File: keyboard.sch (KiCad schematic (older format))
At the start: 80 parts

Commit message: Switch to STM32, wire stuff
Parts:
- gave numbers to parts that had none: 80
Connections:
- net KB_ROW_5: now reaches SW3.1
- net KB_ROW_5: now also SW12.1, SW17.1, SW2.1, SW22.1, SW26.1, SW34.1, SW39.1, SW44.1, SW51.1, SW59.1, SW66.1, SW76.1
- net KB_COL_2: now reaches SW3.2
- net KB_COL_2: now also SW10.2, SW11.2, SW8.2, SW9.2
- net KB_COL_3: now reaches SW12.2
- net KB_COL_3: now also SW13.2, SW14.2, SW15.2, SW16.2
- net KB_COL_4: now reaches SW17.2
- net KB_COL_4: now also SW18.2, SW19.2, SW20.2, SW21.2
- net KB_COL_5: now reaches SW22.2
- net KB_COL_5: now also SW23.2, SW24.2, SW25.2
- net KB_COL_6: now reaches SW26.2
- net KB_COL_6: now also SW27.2, SW28.2, SW29.2, SW30.2
- net KB_COL_7: now reaches SW34.2
- net KB_COL_7: now also SW31.2, SW32.2, SW33.2
- net KB_COL_8: now reaches SW39.2
- net KB_COL_8: now also SW35.2, SW36.2, SW37.2, SW38.2
- net KB_COL_9: now reaches SW44.2
- net KB_COL_9: now also SW40.2, SW41.2, SW42.2, SW43.2
- net KB_ROW_7: now reaches SW4.1
- net KB_ROW_7: now also SW13.1, SW18.1, SW23.1, SW27.1, SW31.1, SW35.1, SW40.1, SW45.1, SW53.1, SW61.1, SW68.1, SW78.1, SW8.1
- net KB_COL_1: now reaches SW4.2
- net KB_COL_1: now also SW2.2, SW5.2, SW6.2, SW7.2
- net KB_COL_10: now reaches SW45.2
- net KB_COL_10: now also SW46.2
- net KB_ROW_8: now reaches SW5.1
- net KB_ROW_8: now also SW14.1, SW19.1, SW24.1, SW28.1, SW32.1, SW36.1, SW41.1, SW54.1, SW62.1, SW69.1, SW79.1, SW9.1
- net KB_ROW_9: now reaches SW6.1
- net KB_ROW_9: now also SW10.1, SW15.1, SW20.1, SW25.1, SW29.1, SW33.1, SW37.1, SW42.1, SW46.1, SW55.1, SW63.1, SW70.1, SW80.1
- net KB_ROW_11: now reaches SW7.1
- net KB_ROW_10: now reaches SW11.1
- net KB_ROW_10: now also SW16.1, SW21.1, SW30.1, SW38.1, SW43.1, SW56.1, SW64.1, SW71.1, SW81.1
- net KB_COL_11: now reaches SW56.2
- net KB_COL_11: now also SW47.2, SW48.2, SW49.2, SW50.2, SW51.2, SW52.2, SW53.2, SW54.2, SW55.2
- net KB_COL_12: now reaches SW64.2
- net KB_COL_12: now also SW57.2, SW58.2, SW59.2, SW60.2, SW61.2, SW62.2, SW63.2
- net KB_COL_13: now reaches SW71.2
- net KB_COL_13: now also SW65.2, SW66.2, SW67.2, SW68.2, SW69.2, SW70.2, SW72.2, SW73.2, SW74.2
- net KB_COL_14: now reaches SW81.2
- net KB_COL_14: now also SW75.2, SW76.2, SW77.2, SW78.2, SW79.2, SW80.2
- net KB_ROW_6: now reaches SW52.1
- net KB_ROW_6: now also SW60.1, SW67.1, SW77.1
- net KB_ROW_4: now reaches SW50.1
- net KB_ROW_4: now also SW74.1
- net KB_ROW_3: now reaches SW49.1
- net KB_ROW_3: now also SW58.1, SW73.1
- net KB_ROW_2: now reaches SW75.1
- net KB_ROW_2: now also SW48.1, SW65.1
- net KB_ROW_1: now reaches SW57.1
- net KB_ROW_1: now also SW47.1, SW72.1
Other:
- note added: "ON button needs its own row for wakeup purpose"
- note removed: "10 cols / 8 rows ?"
- note removed: "ON button : wakeup possible on the ROW output ?\nin that case, 100kOhm pull-down to GND\n\n-> make ON on its own row"
- moved on the sheet: SW10, SW11, SW12, SW13, SW14, SW15, SW16, SW17, SW18, SW19, SW2, SW20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

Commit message: Some updates
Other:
- note removed: "total of 80 keys"
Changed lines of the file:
@@
 	1    0    0    -1
 $EndComp
-Text Notes 1500 6400 0    79   ~ 0
-total of 80 keys
 Text Notes 3450 6750 0    79   ~ 0
 COL are inputs, pull-up sw\nROW output
-Text Notes 1950 7050 0    118  ~ 0
-ON button needs its own row for wakeup purpose
 Text GLabel 1000 4500 0    50   Input ~ 0
 KB_ROW_8
@@
 Text GLabel 1000 5700 0    50   Input ~ 0
 KB_ROW_11
+Text Notes 1950 7050 0    118  ~ 0
+ON button needs its own row for wakeup purpose
 $EndSCHEMATC

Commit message: Assigning footprints
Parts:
- SW10, SW11, SW12, SW13, SW14, SW15, SW16, SW17, SW18, SW19, SW2, SW20, SW21, SW22, SW23, SW24, SW25, SW26, SW27, SW28, SW29, SW3, SW30, SW31, SW32, SW33, SW34, SW35, SW36, SW37, SW38, SW39, SW4, SW40, SW41, SW42, SW43, SW44, SW45, SW46, SW47, SW48, SW49, SW5, SW50, SW51, SW52, SW53, SW54, SW55, SW56, SW57, SW58, SW59, SW6, SW60, SW61, SW62, SW63, SW64, SW65, SW66, SW67, SW68, SW69, SW7, SW70, SW71, SW72, SW73, SW74, SW75, SW76, SW77, SW78, SW79, SW8, SW80, SW81, SW9: footprint (none) -> Button_Switch_THT:SW_PUSH_6mm

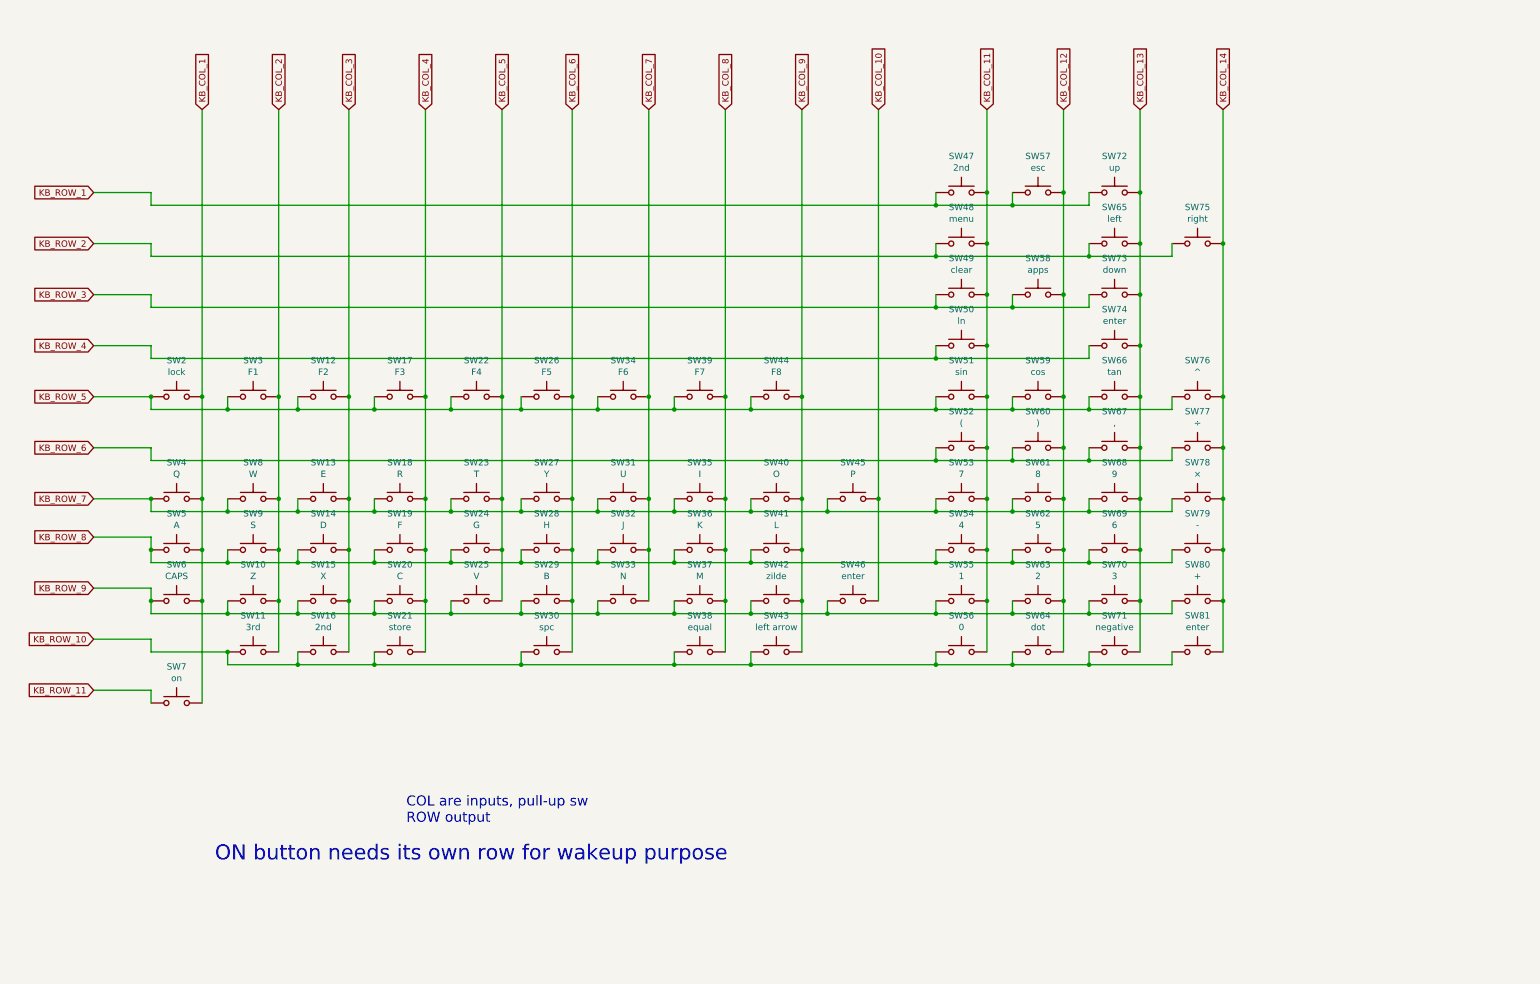
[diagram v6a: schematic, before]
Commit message: Switch keyboard matrix input to a mcp23017
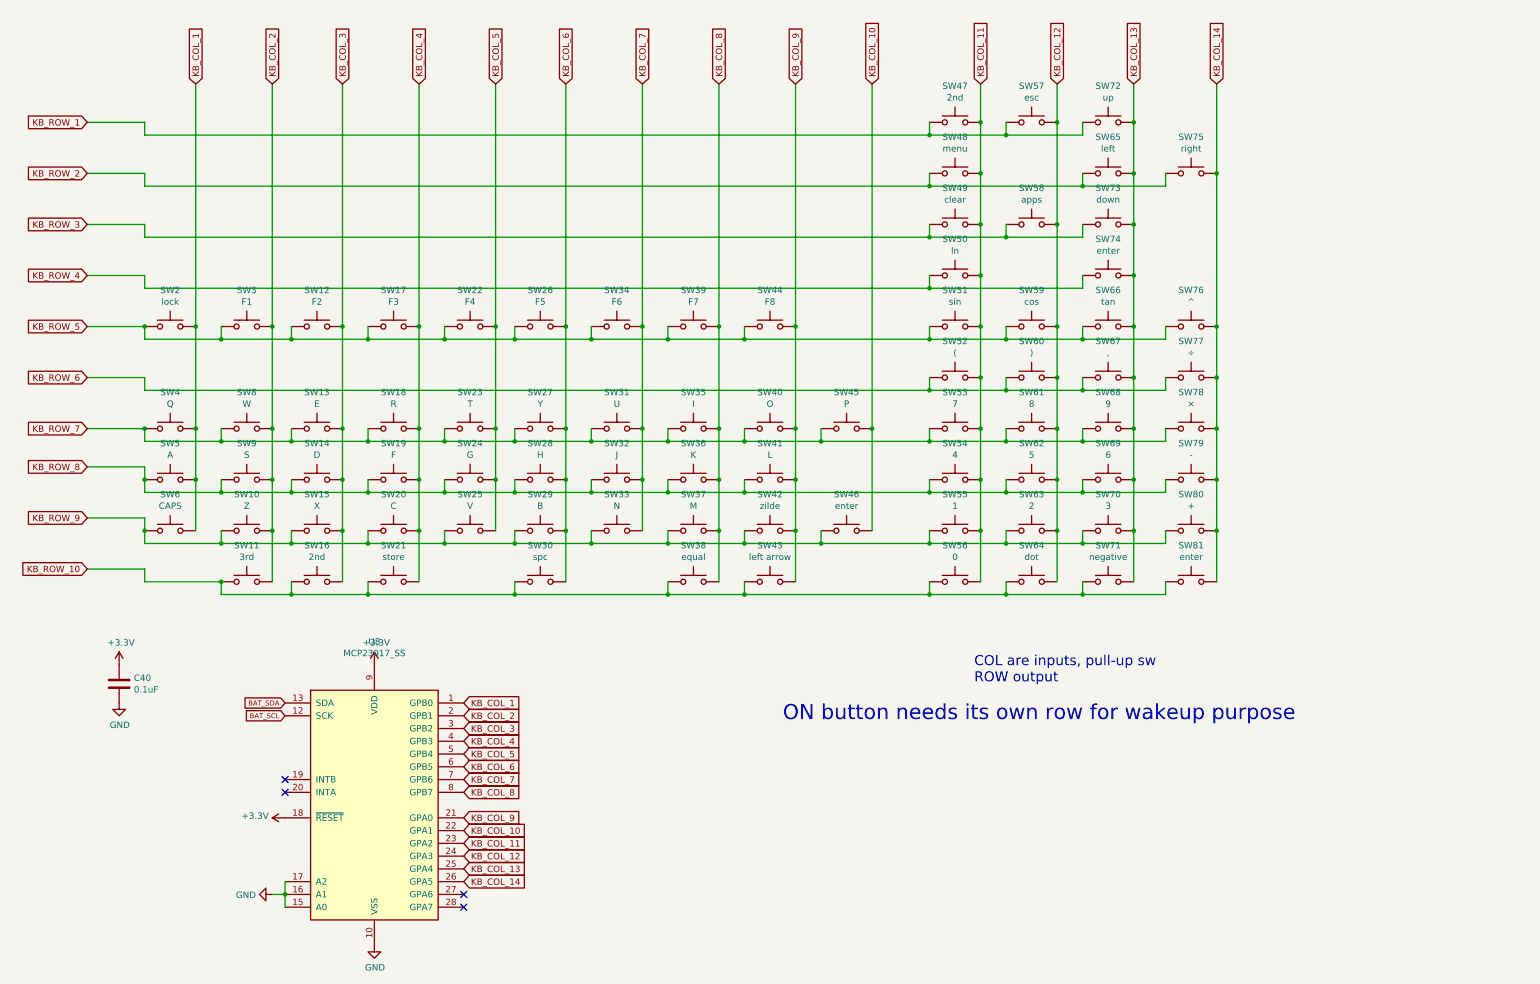
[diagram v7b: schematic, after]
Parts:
- removed SW7: on, Button_Switch_THT:SW_PUSH_6mm, symbol Switch:SW_Push
- added C40: 0.1uF, Capacitor_SMD:C_0805_2012Metric_Pad1.18x1.45mm_HandSolder, symbol Device:C
- added U8: MCP23017_SS, Package_SO:SSOP-28_5.3x10.2mm_P0.65mm, symbol Interface_Expansion:MCP23017_SS
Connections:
- net KB_COL_1: now also U8.1 (GPB0)
- net KB_COL_10: now also U8.22 (GPA1)
- net KB_COL_11: now also U8.23 (GPA2)
- net KB_COL_12: now also U8.24 (GPA3)
- net KB_COL_13: now also U8.25 (GPA4)
- net KB_COL_14: now also U8.26 (GPA5)
- net KB_COL_2: now also U8.2 (GPB1)
- net KB_COL_3: now also U8.3 (GPB2)
- net KB_COL_4: now also U8.4 (GPB3)
- net KB_COL_5: now also U8.5 (GPB4)
- net KB_COL_6: now also U8.6 (GPB5)
- net KB_COL_7: now also U8.7 (GPB6)
- net KB_COL_8: now also U8.8 (GPB7)
- net KB_COL_9: now also U8.21 (GPA0)
- new net +3V3: C40.1, U8.18 (~RESET~), U8.9 (VDD)
- new net BAT_SCL: U8.12 (SCK)
- new net BAT_SDA: U8.13 (SDA)
- new net GND: C40.2, U8.10 (VSS), U8.15 (A0), U8.16 (A1), U8.17 (A2)
- no-connect marks 0 -> 4
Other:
- moved on the sheet: SW10, SW11, SW12, SW13, SW14, SW15, SW16, SW17, SW18, SW19, SW2, SW20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

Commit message: Switch matrix to definitive switch
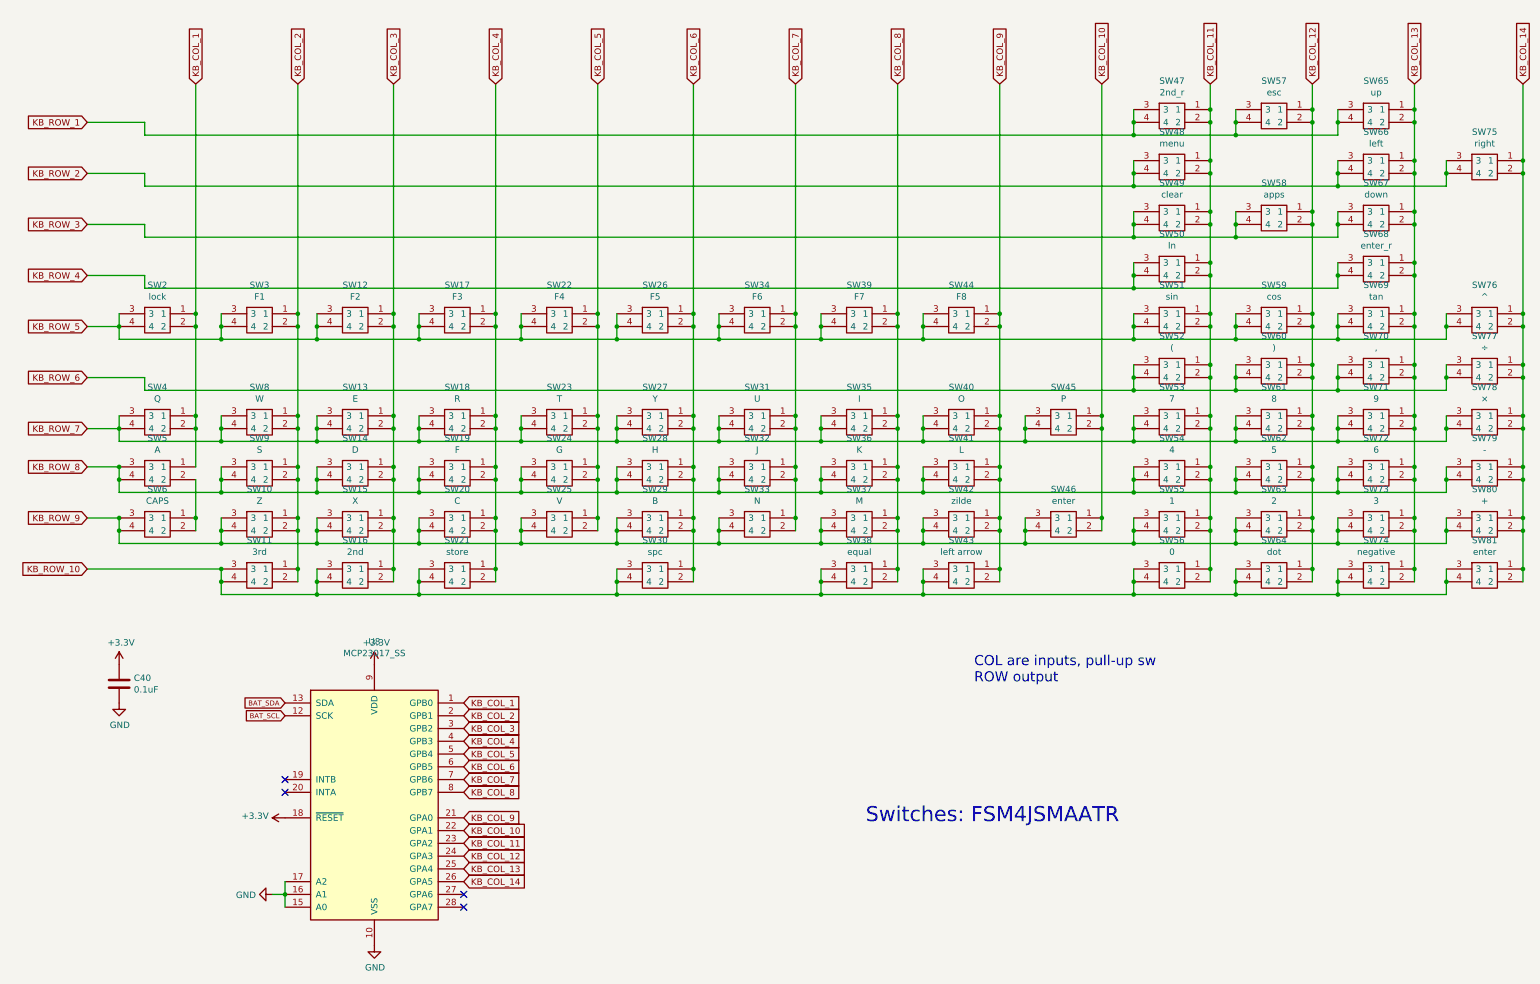
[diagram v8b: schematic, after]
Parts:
- removed SW10: Z, Button_Switch_THT:SW_PUSH_6mm, symbol Switch:SW_Push
- removed SW11: 3rd, Button_Switch_THT:SW_PUSH_6mm, symbol Switch:SW_Push
- removed SW12: F2, Button_Switch_THT:SW_PUSH_6mm, symbol Switch:SW_Push
- removed SW13: E, Button_Switch_THT:SW_PUSH_6mm, symbol Switch:SW_Push
- removed SW14: D, Button_Switch_THT:SW_PUSH_6mm, symbol Switch:SW_Push
- removed SW15: X, Button_Switch_THT:SW_PUSH_6mm, symbol Switch:SW_Push
- removed SW16, SW47: 2nd, Button_Switch_THT:SW_PUSH_6mm, symbol Switch:SW_Push
- removed SW17: F3, Button_Switch_THT:SW_PUSH_6mm, symbol Switch:SW_Push
- removed SW18: R, Button_Switch_THT:SW_PUSH_6mm, symbol Switch:SW_Push
- removed SW19: F, Button_Switch_THT:SW_PUSH_6mm, symbol Switch:SW_Push
- removed SW2: lock, Button_Switch_THT:SW_PUSH_6mm, symbol Switch:SW_Push
- removed SW20: C, Button_Switch_THT:SW_PUSH_6mm, symbol Switch:SW_Push
- removed SW21: store, Button_Switch_THT:SW_PUSH_6mm, symbol Switch:SW_Push
- removed SW22: F4, Button_Switch_THT:SW_PUSH_6mm, symbol Switch:SW_Push
- removed SW23: T, Button_Switch_THT:SW_PUSH_6mm, symbol Switch:SW_Push
- removed SW24: G, Button_Switch_THT:SW_PUSH_6mm, symbol Switch:SW_Push
- removed SW25: V, Button_Switch_THT:SW_PUSH_6mm, symbol Switch:SW_Push
- removed SW26: F5, Button_Switch_THT:SW_PUSH_6mm, symbol Switch:SW_Push
- removed SW27: Y, Button_Switch_THT:SW_PUSH_6mm, symbol Switch:SW_Push
- removed SW28: H, Button_Switch_THT:SW_PUSH_6mm, symbol Switch:SW_Push
- removed SW29: B, Button_Switch_THT:SW_PUSH_6mm, symbol Switch:SW_Push
- removed SW3: F1, Button_Switch_THT:SW_PUSH_6mm, symbol Switch:SW_Push
- removed SW30: spc, Button_Switch_THT:SW_PUSH_6mm, symbol Switch:SW_Push
- removed SW31: U, Button_Switch_THT:SW_PUSH_6mm, symbol Switch:SW_Push
- removed SW32: J, Button_Switch_THT:SW_PUSH_6mm, symbol Switch:SW_Push
- removed SW33: N, Button_Switch_THT:SW_PUSH_6mm, symbol Switch:SW_Push
- removed SW34: F6, Button_Switch_THT:SW_PUSH_6mm, symbol Switch:SW_Push
- removed SW35: I, Button_Switch_THT:SW_PUSH_6mm, symbol Switch:SW_Push
- removed SW36: K, Button_Switch_THT:SW_PUSH_6mm, symbol Switch:SW_Push
- removed SW37: M, Button_Switch_THT:SW_PUSH_6mm, symbol Switch:SW_Push
- removed SW38: equal, Button_Switch_THT:SW_PUSH_6mm, symbol Switch:SW_Push
- removed SW39: F7, Button_Switch_THT:SW_PUSH_6mm, symbol Switch:SW_Push
- removed SW4: Q, Button_Switch_THT:SW_PUSH_6mm, symbol Switch:SW_Push
- removed SW40: O, Button_Switch_THT:SW_PUSH_6mm, symbol Switch:SW_Push
- removed SW41: L, Button_Switch_THT:SW_PUSH_6mm, symbol Switch:SW_Push
- removed SW42: zilde, Button_Switch_THT:SW_PUSH_6mm, symbol Switch:SW_Push
- removed SW43: left arrow, Button_Switch_THT:SW_PUSH_6mm, symbol Switch:SW_Push
- removed SW44: F8, Button_Switch_THT:SW_PUSH_6mm, symbol Switch:SW_Push
- removed SW45: P, Button_Switch_THT:SW_PUSH_6mm, symbol Switch:SW_Push
- removed SW46, SW74, SW81: enter, Button_Switch_THT:SW_PUSH_6mm, symbol Switch:SW_Push
- removed SW48: menu, Button_Switch_THT:SW_PUSH_6mm, symbol Switch:SW_Push
- removed SW49: clear, Button_Switch_THT:SW_PUSH_6mm, symbol Switch:SW_Push
- removed SW5: A, Button_Switch_THT:SW_PUSH_6mm, symbol Switch:SW_Push
- removed SW50: ln, Button_Switch_THT:SW_PUSH_6mm, symbol Switch:SW_Push
- removed SW51: sin, Button_Switch_THT:SW_PUSH_6mm, symbol Switch:SW_Push
- removed SW52: (, Button_Switch_THT:SW_PUSH_6mm, symbol Switch:SW_Push
- removed SW53: 7, Button_Switch_THT:SW_PUSH_6mm, symbol Switch:SW_Push
- removed SW54: 4, Button_Switch_THT:SW_PUSH_6mm, symbol Switch:SW_Push
- removed SW55: 1, Button_Switch_THT:SW_PUSH_6mm, symbol Switch:SW_Push
- removed SW56: 0, Button_Switch_THT:SW_PUSH_6mm, symbol Switch:SW_Push
- removed SW57: esc, Button_Switch_THT:SW_PUSH_6mm, symbol Switch:SW_Push
- removed SW58: apps, Button_Switch_THT:SW_PUSH_6mm, symbol Switch:SW_Push
- removed SW59: cos, Button_Switch_THT:SW_PUSH_6mm, symbol Switch:SW_Push
- removed SW6: CAPS, Button_Switch_THT:SW_PUSH_6mm, symbol Switch:SW_Push
- removed SW60: ), Button_Switch_THT:SW_PUSH_6mm, symbol Switch:SW_Push
- removed SW61: 8, Button_Switch_THT:SW_PUSH_6mm, symbol Switch:SW_Push
- removed SW62: 5, Button_Switch_THT:SW_PUSH_6mm, symbol Switch:SW_Push
- removed SW63: 2, Button_Switch_THT:SW_PUSH_6mm, symbol Switch:SW_Push
- removed SW64: dot, Button_Switch_THT:SW_PUSH_6mm, symbol Switch:SW_Push
- removed SW65: left, Button_Switch_THT:SW_PUSH_6mm, symbol Switch:SW_Push
- removed SW66: tan, Button_Switch_THT:SW_PUSH_6mm, symbol Switch:SW_Push
- removed SW67: ,, Button_Switch_THT:SW_PUSH_6mm, symbol Switch:SW_Push
- removed SW68: 9, Button_Switch_THT:SW_PUSH_6mm, symbol Switch:SW_Push
- removed SW69: 6, Button_Switch_THT:SW_PUSH_6mm, symbol Switch:SW_Push
- removed SW70: 3, Button_Switch_THT:SW_PUSH_6mm, symbol Switch:SW_Push
- removed SW71: negative, Button_Switch_THT:SW_PUSH_6mm, symbol Switch:SW_Push
- removed SW72: up, Button_Switch_THT:SW_PUSH_6mm, symbol Switch:SW_Push
- removed SW73: down, Button_Switch_THT:SW_PUSH_6mm, symbol Switch:SW_Push
- removed SW75: right, Button_Switch_THT:SW_PUSH_6mm, symbol Switch:SW_Push
- removed SW76: ^, Button_Switch_THT:SW_PUSH_6mm, symbol Switch:SW_Push
- removed SW77: ÷, Button_Switch_THT:SW_PUSH_6mm, symbol Switch:SW_Push
- removed SW78: ×, Button_Switch_THT:SW_PUSH_6mm, symbol Switch:SW_Push
- removed SW79: -, Button_Switch_THT:SW_PUSH_6mm, symbol Switch:SW_Push
- removed SW8: W, Button_Switch_THT:SW_PUSH_6mm, symbol Switch:SW_Push
- removed SW80: +, Button_Switch_THT:SW_PUSH_6mm, symbol Switch:SW_Push
- removed SW9: S, Button_Switch_THT:SW_PUSH_6mm, symbol Switch:SW_Push
- added SW10: Z, SamacSys_Parts:FSM4JSMATR, symbol SamacSys_Parts:FSM4JSMAATR
- added SW11: 3rd, SamacSys_Parts:FSM4JSMATR, symbol SamacSys_Parts:FSM4JSMAATR
- added SW12: F2, SamacSys_Parts:FSM4JSMATR, symbol SamacSys_Parts:FSM4JSMAATR
- added SW13: E, SamacSys_Parts:FSM4JSMATR, symbol SamacSys_Parts:FSM4JSMAATR
- added SW14: D, SamacSys_Parts:FSM4JSMATR, symbol SamacSys_Parts:FSM4JSMAATR
- added SW15: X, SamacSys_Parts:FSM4JSMATR, symbol SamacSys_Parts:FSM4JSMAATR
- added SW16: 2nd, SamacSys_Parts:FSM4JSMATR, symbol SamacSys_Parts:FSM4JSMAATR
- added SW17: F3, SamacSys_Parts:FSM4JSMATR, symbol SamacSys_Parts:FSM4JSMAATR
- added SW18: R, SamacSys_Parts:FSM4JSMATR, symbol SamacSys_Parts:FSM4JSMAATR
- added SW19: F, SamacSys_Parts:FSM4JSMATR, symbol SamacSys_Parts:FSM4JSMAATR
- added SW2: lock, SamacSys_Parts:FSM4JSMATR, symbol SamacSys_Parts:FSM4JSMAATR
- added SW20: C, SamacSys_Parts:FSM4JSMATR, symbol SamacSys_Parts:FSM4JSMAATR
- added SW21: store, SamacSys_Parts:FSM4JSMATR, symbol SamacSys_Parts:FSM4JSMAATR
- added SW22: F4, SamacSys_Parts:FSM4JSMATR, symbol SamacSys_Parts:FSM4JSMAATR
- added SW23: T, SamacSys_Parts:FSM4JSMATR, symbol SamacSys_Parts:FSM4JSMAATR
- added SW24: G, SamacSys_Parts:FSM4JSMATR, symbol SamacSys_Parts:FSM4JSMAATR
- added SW25: V, SamacSys_Parts:FSM4JSMATR, symbol SamacSys_Parts:FSM4JSMAATR
- added SW26: F5, SamacSys_Parts:FSM4JSMATR, symbol SamacSys_Parts:FSM4JSMAATR
- added SW27: Y, SamacSys_Parts:FSM4JSMATR, symbol SamacSys_Parts:FSM4JSMAATR
- added SW28: H, SamacSys_Parts:FSM4JSMATR, symbol SamacSys_Parts:FSM4JSMAATR
- added SW29: B, SamacSys_Parts:FSM4JSMATR, symbol SamacSys_Parts:FSM4JSMAATR
- added SW3: F1, SamacSys_Parts:FSM4JSMATR, symbol SamacSys_Parts:FSM4JSMAATR
- added SW30: spc, SamacSys_Parts:FSM4JSMATR, symbol SamacSys_Parts:FSM4JSMAATR
- added SW31: U, SamacSys_Parts:FSM4JSMATR, symbol SamacSys_Parts:FSM4JSMAATR
- added SW32: J, SamacSys_Parts:FSM4JSMATR, symbol SamacSys_Parts:FSM4JSMAATR
- added SW33: N, SamacSys_Parts:FSM4JSMATR, symbol SamacSys_Parts:FSM4JSMAATR
- added SW34: F6, SamacSys_Parts:FSM4JSMATR, symbol SamacSys_Parts:FSM4JSMAATR
- added SW35: I, SamacSys_Parts:FSM4JSMATR, symbol SamacSys_Parts:FSM4JSMAATR
- added SW36: K, SamacSys_Parts:FSM4JSMATR, symbol SamacSys_Parts:FSM4JSMAATR
- added SW37: M, SamacSys_Parts:FSM4JSMATR, symbol SamacSys_Parts:FSM4JSMAATR
- added SW38: equal, SamacSys_Parts:FSM4JSMATR, symbol SamacSys_Parts:FSM4JSMAATR
- added SW39: F7, SamacSys_Parts:FSM4JSMATR, symbol SamacSys_Parts:FSM4JSMAATR
- added SW4: Q, SamacSys_Parts:FSM4JSMATR, symbol SamacSys_Parts:FSM4JSMAATR
- added SW40: O, SamacSys_Parts:FSM4JSMATR, symbol SamacSys_Parts:FSM4JSMAATR
- added SW41: L, SamacSys_Parts:FSM4JSMATR, symbol SamacSys_Parts:FSM4JSMAATR
- added SW42: zilde, SamacSys_Parts:FSM4JSMATR, symbol SamacSys_Parts:FSM4JSMAATR
- added SW43: left arrow, SamacSys_Parts:FSM4JSMATR, symbol SamacSys_Parts:FSM4JSMAATR
- added SW44: F8, SamacSys_Parts:FSM4JSMATR, symbol SamacSys_Parts:FSM4JSMAATR
- added SW45: P, SamacSys_Parts:FSM4JSMATR, symbol SamacSys_Parts:FSM4JSMAATR
- added SW46, SW81: enter, SamacSys_Parts:FSM4JSMATR, symbol SamacSys_Parts:FSM4JSMAATR
- added SW47: 2nd_r, SamacSys_Parts:FSM4JSMATR, symbol SamacSys_Parts:FSM4JSMAATR
- added SW48: menu, SamacSys_Parts:FSM4JSMATR, symbol SamacSys_Parts:FSM4JSMAATR
- added SW49: clear, SamacSys_Parts:FSM4JSMATR, symbol SamacSys_Parts:FSM4JSMAATR
- added SW5: A, SamacSys_Parts:FSM4JSMATR, symbol SamacSys_Parts:FSM4JSMAATR
- added SW50: ln, SamacSys_Parts:FSM4JSMATR, symbol SamacSys_Parts:FSM4JSMAATR
- added SW51: sin, SamacSys_Parts:FSM4JSMATR, symbol SamacSys_Parts:FSM4JSMAATR
- added SW52: (, SamacSys_Parts:FSM4JSMATR, symbol SamacSys_Parts:FSM4JSMAATR
- added SW53: 7, SamacSys_Parts:FSM4JSMATR, symbol SamacSys_Parts:FSM4JSMAATR
- added SW54: 4, SamacSys_Parts:FSM4JSMATR, symbol SamacSys_Parts:FSM4JSMAATR
- added SW55: 1, SamacSys_Parts:FSM4JSMATR, symbol SamacSys_Parts:FSM4JSMAATR
- added SW56: 0, SamacSys_Parts:FSM4JSMATR, symbol SamacSys_Parts:FSM4JSMAATR
- added SW57: esc, SamacSys_Parts:FSM4JSMATR, symbol SamacSys_Parts:FSM4JSMAATR
- added SW58: apps, SamacSys_Parts:FSM4JSMATR, symbol SamacSys_Parts:FSM4JSMAATR
- added SW59: cos, SamacSys_Parts:FSM4JSMATR, symbol SamacSys_Parts:FSM4JSMAATR
- added SW6: CAPS, SamacSys_Parts:FSM4JSMATR, symbol SamacSys_Parts:FSM4JSMAATR
- added SW60: ), SamacSys_Parts:FSM4JSMATR, symbol SamacSys_Parts:FSM4JSMAATR
- added SW61: 8, SamacSys_Parts:FSM4JSMATR, symbol SamacSys_Parts:FSM4JSMAATR
- added SW62: 5, SamacSys_Parts:FSM4JSMATR, symbol SamacSys_Parts:FSM4JSMAATR
- added SW63: 2, SamacSys_Parts:FSM4JSMATR, symbol SamacSys_Parts:FSM4JSMAATR
- added SW64: dot, SamacSys_Parts:FSM4JSMATR, symbol SamacSys_Parts:FSM4JSMAATR
- added SW65: up, SamacSys_Parts:FSM4JSMATR, symbol SamacSys_Parts:FSM4JSMAATR
- added SW66: left, SamacSys_Parts:FSM4JSMATR, symbol SamacSys_Parts:FSM4JSMAATR
- added SW67: down, SamacSys_Parts:FSM4JSMATR, symbol SamacSys_Parts:FSM4JSMAATR
- added SW68: enter_r, SamacSys_Parts:FSM4JSMATR, symbol SamacSys_Parts:FSM4JSMAATR
- added SW69: tan, SamacSys_Parts:FSM4JSMATR, symbol SamacSys_Parts:FSM4JSMAATR
- added SW70: ,, SamacSys_Parts:FSM4JSMATR, symbol SamacSys_Parts:FSM4JSMAATR
- added SW71: 9, SamacSys_Parts:FSM4JSMATR, symbol SamacSys_Parts:FSM4JSMAATR
- added SW72: 6, SamacSys_Parts:FSM4JSMATR, symbol SamacSys_Parts:FSM4JSMAATR
- added SW73: 3, SamacSys_Parts:FSM4JSMATR, symbol SamacSys_Parts:FSM4JSMAATR
- added SW74: negative, SamacSys_Parts:FSM4JSMATR, symbol SamacSys_Parts:FSM4JSMAATR
- added SW75: right, SamacSys_Parts:FSM4JSMATR, symbol SamacSys_Parts:FSM4JSMAATR
- added SW76: ^, SamacSys_Parts:FSM4JSMATR, symbol SamacSys_Parts:FSM4JSMAATR
- added SW77: ÷, SamacSys_Parts:FSM4JSMATR, symbol SamacSys_Parts:FSM4JSMAATR
- added SW78: ×, SamacSys_Parts:FSM4JSMATR, symbol SamacSys_Parts:FSM4JSMAATR
- added SW79: -, SamacSys_Parts:FSM4JSMATR, symbol SamacSys_Parts:FSM4JSMAATR
- added SW8: W, SamacSys_Parts:FSM4JSMATR, symbol SamacSys_Parts:FSM4JSMAATR
- added SW80: +, SamacSys_Parts:FSM4JSMATR, symbol SamacSys_Parts:FSM4JSMAATR
- added SW9: S, SamacSys_Parts:FSM4JSMATR, symbol SamacSys_Parts:FSM4JSMAATR
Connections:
- net KB_COL_1: now also SW2.1, SW2.2, SW4.1, SW4.2, SW5.1
- net KB_COL_10: now also SW45.1, SW45.2, SW46.1, SW46.2
- net KB_COL_11: now also SW47.1, SW47.2, SW48.1, SW48.2, SW49.1, SW49.2, SW50.1, SW50.2, SW51.1, SW51.2, SW52.1, SW52.2, SW53.1, SW53.2, SW54.1, SW54.2, SW55.1, SW55.2, SW56.1, SW56.2
- net KB_COL_12: now also SW57.1, SW57.2, SW58.1, SW58.2, SW59.1, SW59.2, SW60.1, SW60.2, SW61.1, SW61.2, SW62.1, SW62.2, SW63.1, SW63.2, SW64.1, SW64.2
- net KB_COL_13: now also SW65.1, SW65.2, SW66.1, SW66.2, SW67.1, SW67.2, SW68.1, SW68.2, SW69.1, SW69.2, SW70.1, SW70.2, SW71.1, SW71.2, SW72.1, SW72.2, SW73.1, SW73.2, SW74.1, SW74.2
- net KB_COL_14: now also SW75.1, SW75.2, SW76.1, SW76.2, SW77.1, SW77.2, SW78.1, SW78.2, SW79.1, SW79.2, SW80.1, SW80.2, SW81.1, SW81.2
- net KB_COL_2: now also SW10.1, SW10.2, SW11.1, SW11.2, SW3.1, SW3.2, SW8.1, SW8.2, SW9.1, SW9.2
- net KB_COL_3: now also SW12.1, SW12.2, SW13.1, SW13.2, SW14.1, SW14.2, SW15.1, SW15.2, SW16.1, SW16.2
- net KB_COL_4: now also SW17.1, SW17.2, SW18.1, SW18.2, SW19.1, SW19.2, SW20.1, SW20.2, SW21.1, SW21.2
- net KB_COL_5: now also SW22.1, SW22.2, SW23.1, SW23.2, SW24.1, SW24.2, SW25.1, SW25.2
- net KB_COL_6: now also SW26.1, SW26.2, SW27.1, SW27.2, SW28.1, SW28.2, SW29.1, SW29.2, SW30.1, SW30.2
- net KB_COL_7: now also SW31.1, SW31.2, SW32.1, SW32.2, SW33.1, SW33.2, SW34.1, SW34.2
- net KB_COL_8: now also SW35.1, SW35.2, SW36.1, SW36.2, SW37.1, SW37.2, SW38.1, SW38.2, SW39.1, SW39.2
- net KB_COL_9: now also SW40.1, SW40.2, SW41.1, SW41.2, SW42.1, SW42.2, SW43.1, SW43.2, SW44.1, SW44.2
- net KB_ROW_1: now also SW47.3, SW47.4, SW57.3, SW57.4, SW65.3, SW65.4
- net KB_ROW_10: now also SW11.3, SW11.4, SW16.3, SW16.4, SW21.3, SW21.4, SW30.3, SW30.4, SW38.3, SW38.4, SW43.3, SW43.4, SW56.3, SW56.4, SW64.3, SW64.4, SW74.3, SW74.4, SW81.3, SW81.4
- net KB_ROW_2: now also SW48.3, SW48.4, SW66.3, SW66.4, SW75.3, SW75.4
- net KB_ROW_3: now also SW49.3, SW49.4, SW58.3, SW58.4, SW67.3, SW67.4
- net KB_ROW_4: now also SW50.3, SW50.4, SW68.3, SW68.4
- net KB_ROW_5: now also SW12.3, SW12.4, SW17.3, SW17.4, SW2.3, SW2.4, SW22.3, SW22.4, SW26.3, SW26.4, SW3.3, SW3.4, SW34.3, SW34.4, SW39.3, SW39.4, SW44.3, SW44.4, SW51.3, SW51.4, SW59.3, SW59.4, SW69.3, SW69.4, SW76.3, SW76.4
- net KB_ROW_6: now also SW52.3, SW52.4, SW60.3, SW60.4, SW70.3, SW70.4, SW77.3, SW77.4
- net KB_ROW_7: now also SW13.3, SW13.4, SW18.3, SW18.4, SW23.3, SW23.4, SW27.3, SW27.4, SW31.3, SW31.4, SW35.3, SW35.4, SW4.3, SW4.4, SW40.3, SW40.4, SW45.3, SW45.4, SW53.3, SW53.4, SW61.3, SW61.4, SW71.3, SW71.4, SW78.3, SW78.4, SW8.3, SW8.4
- net KB_ROW_8: now also SW14.3, SW14.4, SW19.3, SW19.4, SW24.3, SW24.4, SW28.3, SW28.4, SW32.3, SW32.4, SW36.3, SW36.4, SW41.3, SW41.4, SW5.3, SW5.4, SW54.3, SW54.4, SW62.3, SW62.4, SW72.3, SW72.4, SW79.3, SW79.4, SW9.3, SW9.4
- net KB_ROW_9: now also SW10.3, SW10.4, SW15.3, SW15.4, SW20.3, SW20.4, SW25.3, SW25.4, SW29.3, SW29.4, SW33.3, SW33.4, SW37.3, SW37.4, SW42.3, SW42.4, SW46.3, SW46.4, SW55.3, SW55.4, SW6.3, SW6.4, SW63.3, SW63.4, SW73.3, SW73.4, SW80.3, SW80.4
- new net: SW5.2, SW6.1, SW6.2
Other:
- note added: "Switches: FSM4JSMAATR"
- note removed: "ON button needs its own row for wakeup purpose"
